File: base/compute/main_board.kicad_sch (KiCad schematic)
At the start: 18 parts, among them J1 USB_C_Receptacle_USB2.0_16P, J3 Conn_02x20_Counter_Clockwise, U1 MCP1700T-1202ETT, U3 LD1117S33TR_SOT223

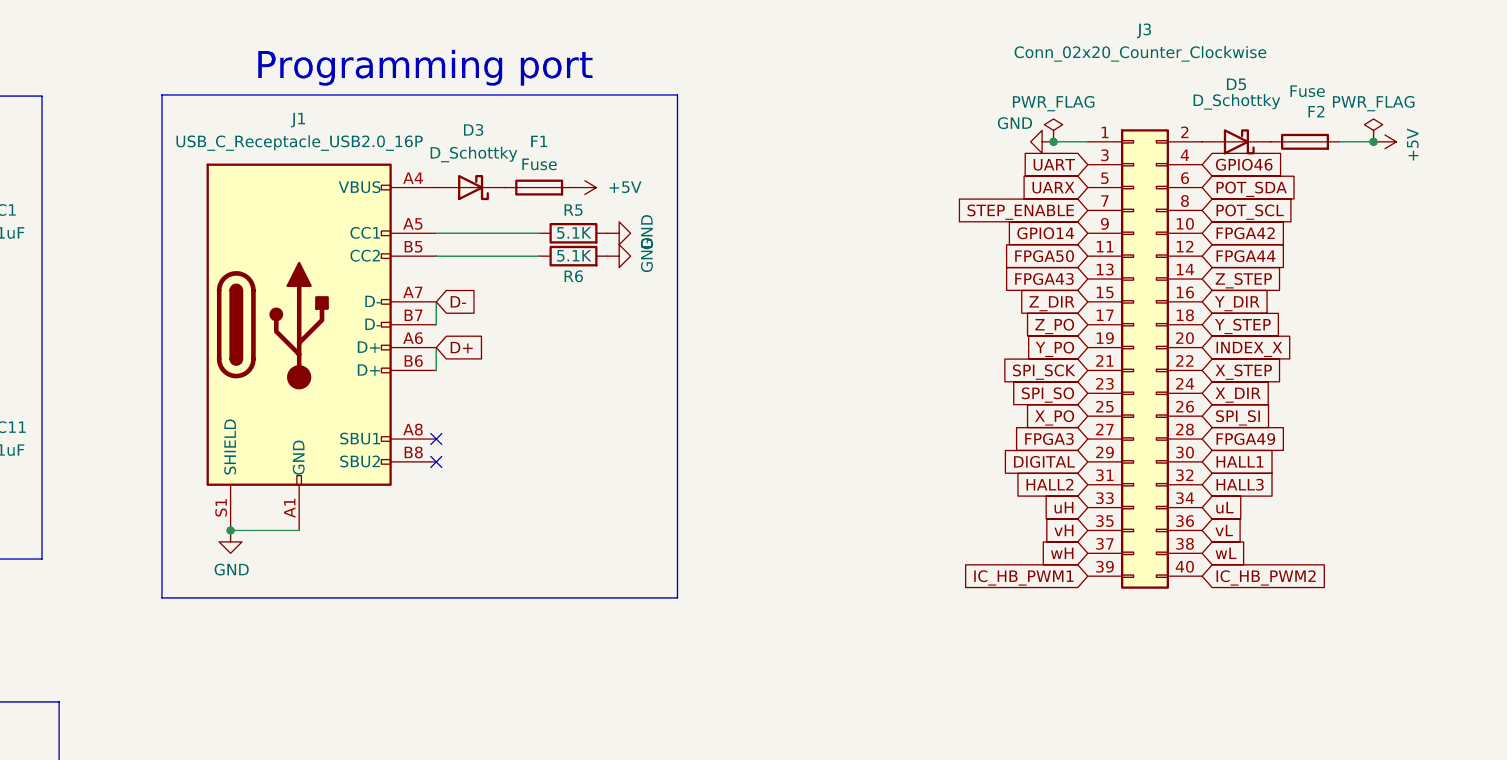
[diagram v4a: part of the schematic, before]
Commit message: fixed boms, small modifications to the boards.
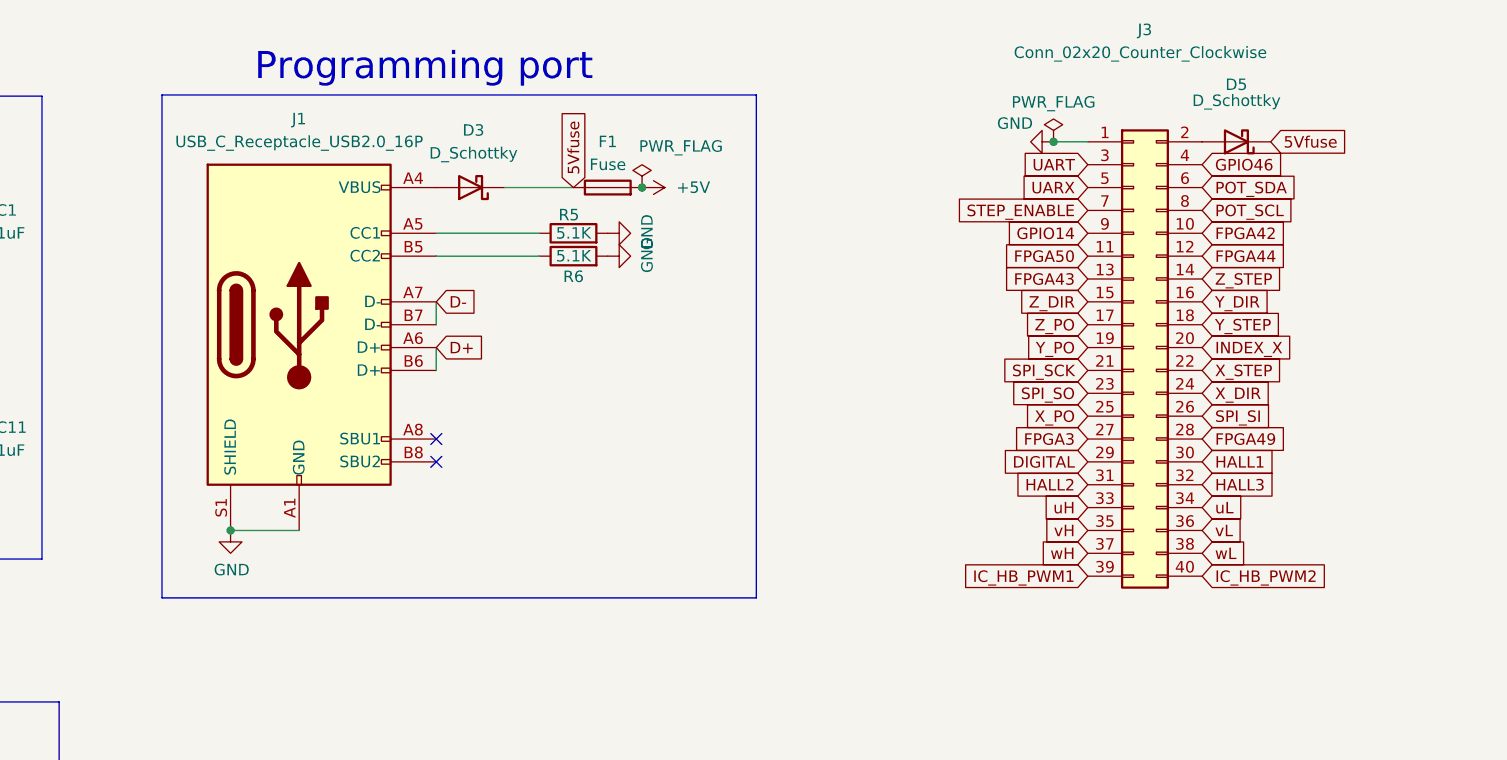
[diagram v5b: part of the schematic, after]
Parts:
- removed F2: Fuse, Fuse:Fuse_0402_1005Metric_Pad0.77x0.64mm_HandSolder, symbol Device:Fuse
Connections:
- net 5Vfuse: now reaches D5.1 (K)
- net 5Vfuse: now also D3.1 (K), F1.1
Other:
- moved on the sheet: F1
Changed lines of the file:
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@@
 	)
 	(junction
-		(at 121.92 77.47)
+		(at 167.64 39.37)
 		(diameter 0)
 		(color 0 0 0 0)
 	)
 	(junction
-		(at 248.92 34.29)
+		(at 121.92 77.47)
 		(diameter 0)
 		(color 0 0 0 0)
@@
 	(wire
 		(pts
-			(xy 248.92 34.29) (xy 245.11 34.29)
+			(xy 152.4 39.37) (xy 160.02 39.37)
 		)
 		(stroke
@@
 	(rectangle
 		(start 114.3 29.083)
-		(end 171.577 84.963)
+		(end 180.34 84.963)
 		(stroke
 			(width 0)
@@
 		)
 	)
+	(global_label "5Vfuse"
+		(shape input)
+		(at 237.49 34.29 0)
+		(fields_autoplaced yes)
+		(effects
+			(font
+				(size 1.27 1.27)
+			)
+			(justify left)
+		)
+		(property "Intersheetrefs" "${INTERSHEET_REFS}"
+			(at 246.1105 34.29 0)
+			(effects
+				(font
+					(size 1.27 1.27)
+				)
+				(justify left)
+				(hide yes)
+			)
+		)
+	)
+	(global_label "5Vfuse"
+		(shape input)
+		(at 160.02 39.37 90)
+		(fields_autoplaced yes)
+		(effects
+			(font
+				(size 1.27 1.27)
+			)
+			(justify left)
+		)
+		(property "Intersheetrefs" "${INTERSHEET_REFS}"
+			(at 160.02 30.7495 90)
+			(effects
+				(font
+					(size 1.27 1.27)
+				)
+				(justify left)
+				(hide yes)
+			)
+		)
+	)
 	(global_label "SPI_SO"
 		(shape input)
@@
 	)
 	(symbol
-		(lib_id "Device:Fuse")
-		(at 241.3 34.29 90)
-		(unit 1)
-		(exclude_from_sim no)
-		(in_bom yes)
-		(on_board yes)
-		(dnp no)
-		(property "Reference" "F2"
-			(at 242.57 30.988 90)
-			(effects
-				(font
-					(size 1.27 1.27)
-				)
-			)
-		)
-		(property "Value" "Fuse"
-			(at 241.554 28.702 90)
-			(effects
-				(font
-					(size 1.27 1.27)
-				)
-			)
-		)
-		(property "Footprint" "Fuse:Fuse_0402_1005Metric_Pad0.77x0.64mm_HandSolder"
-			(at 241.3 36.068 90)
-			(effects
-				(font
-					(size 1.27 1.27)
-				)
-				(hide yes)
-			)
-		)
-		(property "Datasheet" ""
-			(at 241.3 34.29 0)
-			(effects
-				(font
-					(size 1.27 1.27)
-				)
-				(hide yes)
-			)
-		)
-		(property "Description" ""
-			(at 241.3 34.29 0)
-			(effects
-				(font
-					(size 1.27 1.27)
-				)
-				(hide yes)
-			)
-		)
-		(property "farnell#" "2799448"
-			(at 241.3 34.29 90)
-			(effects
-				(font
-					(size 1.27 1.27)
-				)
-				(hide yes)
-			)
-		)
-		(property "manf#" "SF-0402FP100-2"
-			(at 241.3 34.29 90)
-			(effects
-				(font
-					(size 1.27 1.27)
-				)
-				(hide yes)
-			)
-		)
-		(property "mouser#" "652-SF-0402FP100-2"
-			(at 241.3 34.29 90)
-			(effects
-				(font
-					(size 1.27 1.27)
-				)
-				(hide yes)
-			)
-		)
-		(pin "1"
-		)
-		(pin "2"
-		)
-		(instances
-			(project "main_board"
-				(path "/3f5fe6b7-98fc-4d3e-9567-f9f7202d1455"
-					(reference "F2")
-					(unit 1)
-				)
-			)
-		)
-	)
-	(symbol
 		(lib_id "Device:LED_ABGR")
 		(at 82.55 113.03 180)
@@
 		(dnp no)
 		(property "Reference" "R5"
-			(at 160.02 41.91 90)
+			(at 159.512 42.418 90)
 			(effects
 				(font
@@
 	)
 	(symbol
-		(lib_id "power:+5V")
-		(at 248.92 34.29 270)
-		(unit 1)
-		(exclude_from_sim no)
-		(in_bom yes)
-		(on_board yes)
-		(dnp no)
-		(property "Reference" "#PWR01"
-			(at 245.11 34.29 0)
-			(effects
-				(font
-					(size 1.27 1.27)
-				)
-				(hide yes)
-			)
-		)
-		(property "Value" "+5V"
-			(at 253.3142 34.671 0)
-			(effects
-				(font
-					(size 1.27 1.27)
-				)
-			)
-		)
-		(property "Footprint" ""
-			(at 248.92 34.29 0)
-			(effects
-				(font
-					(size 1.27 1.27)
-				)
-				(hide yes)
-			)
-		)
-		(property "Datasheet" ""
-			(at 248.92 34.29 0)
-			(effects
-				(font
-					(size 1.27 1.27)
-				)
-				(hide yes)
-			)
-		)
-		(property "Description" "Power symbol creates a global label with name \"+5V\""
-			(at 248.92 34.29 0)
-			(effects
-				(font
-					(size 1.27 1.27)
-				)
-				(hide yes)
-			)
-		)
-		(pin "1"
-		)
-		(instances
-			(project "main_board"
-				(path "/3f5fe6b7-98fc-4d3e-9567-f9f7202d1455"
-					(reference "#PWR01")
-					(unit 1)
-				)
-			)
-		)
-	)
-	(symbol
 		(lib_id "Device:Fuse")
-		(at 156.21 39.37 90)
+		(at 163.83 39.37 90)
 		(unit 1)
 		(exclude_from_sim no)
@@
 		(fields_autoplaced yes)
 		(property "Reference" "F1"
-			(at 156.21 34.29 90)
+			(at 163.83 34.29 90)
 			(effects
 				(font
@@
 		)
 		(property "Value" "Fuse"
-			(at 156.21 36.83 90)
+			(at 163.83 36.83 90)
 			(effects
 				(font
@@
 		)
 		(property "Footprint" "Fuse:Fuse_0402_1005Metric_Pad0.77x0.64mm_HandSolder"
-			(at 156.21 41.148 90)
+			(at 163.83 41.148 90)
 			(effects
 				(font
@@
 		)
 		(property "Datasheet" ""
-			(at 156.21 39.37 0)
+			(at 163.83 39.37 0)
 			(effects
 				(font
@@
 		)
 		(property "Description" ""
-			(at 156.21 39.37 0)
+			(at 163.83 39.37 0)
 			(effects
 				(font
@@
 		)
 		(property "farnell#" "2799448"
-			(at 156.21 39.37 90)
+			(at 163.83 39.37 90)
 			(effects
 				(font
@@
 		)
 		(property "manf#" "SF-0402FP100-2"
-			(at 156.21 39.37 90)
+			(at 163.83 39.37 90)
 			(effects
 				(font
@@
 		)
 		(property "mouser#" "652-SF-0402FP100-2"
-			(at 156.21 39.37 90)
+			(at 163.83 39.37 90)
 			(effects
 				(font
@@
 	(symbol
 		(lib_id "power:PWR_FLAG")
-		(at 248.92 34.29 0)
+		(at 167.64 39.37 0)
 		(unit 1)
 		(exclude_from_sim no)
@@
 		(dnp no)
 		(property "Reference" "#FLG02"
-			(at 248.92 32.385 0)
+			(at 167.64 37.465 0)
 			(effects
 				(font
@@
 		)
 		(property "Value" "PWR_FLAG"
-			(at 248.92 29.8958 0)
+			(at 171.958 34.798 0)
 			(effects
 				(font
@@
 		)
 		(property "Footprint" ""
-			(at 248.92 34.29 0)
+			(at 167.64 39.37 0)
 			(effects
 				(font
@@
 		)
 		(property "Datasheet" "~"
-			(at 248.92 34.29 0)
+			(at 167.64 39.37 0)
 			(effects
 				(font
@@
 		)
 		(property "Description" "Special symbol for telling ERC where power comes from"
-			(at 248.92 34.29 0)
+			(at 167.64 39.37 0)
 			(effects
 				(font
@@
 	(symbol
 		(lib_id "power:+5V")
-		(at 160.02 39.37 270)
+		(at 167.64 39.37 270)
 		(unit 1)
 		(exclude_from_sim no)
@@
 		(dnp no)
 		(property "Reference" "#PWR03"
-			(at 156.21 39.37 0)
+			(at 163.83 39.37 0)
 			(effects
 				(font
@@
 		)
 		(property "Value" "+5V"
-			(at 163.83 39.37 90)
+			(at 171.45 39.37 90)
 			(effects
 				(font
@@
 		)
 		(property "Footprint" ""
-			(at 160.02 39.37 0)
+			(at 167.64 39.37 0)
 			(effects
 				(font
@@
 		)
 		(property "Datasheet" ""
-			(at 160.02 39.37 0)
+			(at 167.64 39.37 0)
 			(effects
 				(font
@@
 		)
 		(property "Description" "Power symbol creates a global label with name \"+5V\""
-			(at 160.02 39.37 0)
+			(at 167.64 39.37 0)
 			(effects
 				(font

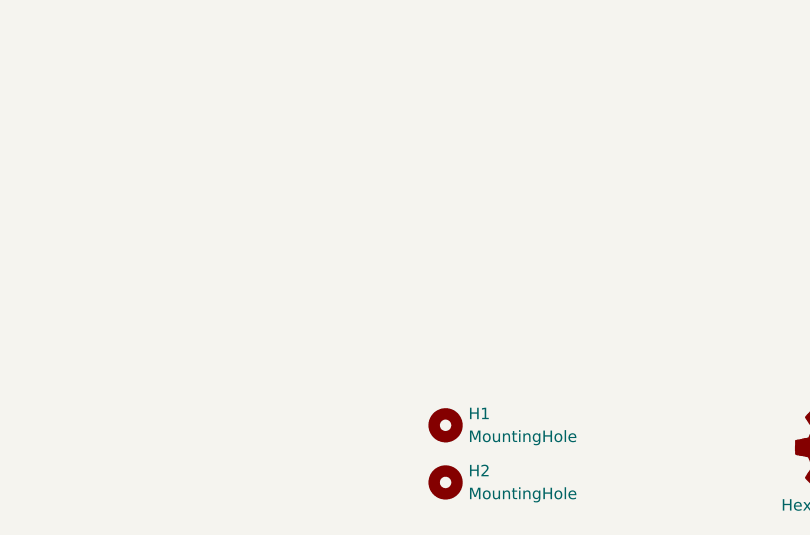
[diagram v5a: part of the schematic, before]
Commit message: added pcb files, added offset between compute and extension
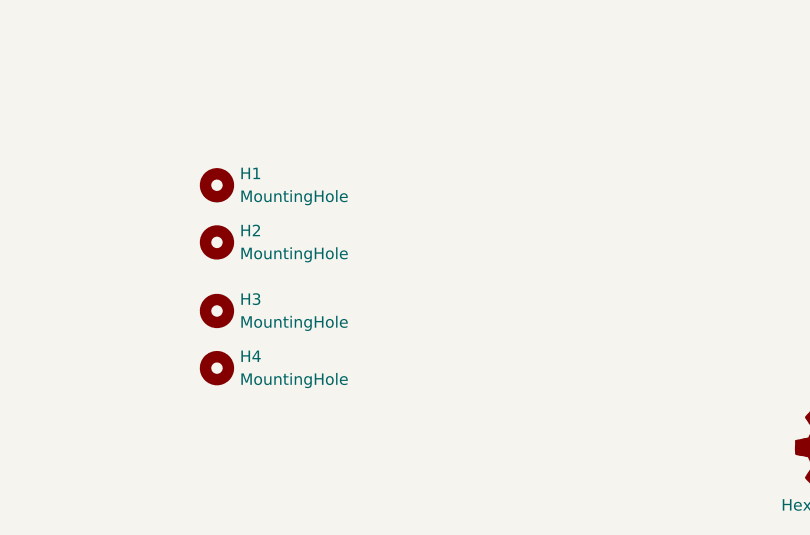
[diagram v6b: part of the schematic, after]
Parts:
- added H3, H4: MountingHole, MountingHole:MountingHole_2.2mm_M2, symbol Mechanical:MountingHole
- H1, H2: footprint MountingHole:MountingHole_3.2mm_M3 -> MountingHole:MountingHole_2.2mm_M2
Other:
- moved on the sheet: H1, H2
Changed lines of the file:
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@@
 	(symbol
 		(lib_id "Mechanical:MountingHole")
-		(at 208.28 148.59 0)
+		(at 182.88 121.92 0)
 		(unit 1)
 		(exclude_from_sim yes)
@@
 		(fields_autoplaced yes)
 		(property "Reference" "H2"
-			(at 210.82 147.3199 0)
+			(at 185.42 120.6499 0)
 			(effects
 				(font
@@
 		)
 		(property "Value" "MountingHole"
-			(at 210.82 149.8599 0)
+			(at 185.42 123.1899 0)
 			(effects
 				(font
@@
 			)
 		)
-		(property "Footprint" "MountingHole:MountingHole_3.2mm_M3"
-			(at 208.28 148.59 0)
+		(property "Footprint" "MountingHole:MountingHole_2.2mm_M2"
+			(at 182.88 121.92 0)
 			(effects
 				(font
@@
 		)
 		(property "Datasheet" "~"
-			(at 208.28 148.59 0)
+			(at 182.88 121.92 0)
 			(effects
 				(font
@@
 		)
 		(property "Description" "Mounting Hole without connection"
-			(at 208.28 148.59 0)
+			(at 182.88 121.92 0)
 			(effects
 				(font
@@
 	(symbol
 		(lib_id "Mechanical:MountingHole")
-		(at 208.28 142.24 0)
+		(at 182.88 129.54 0)
 		(unit 1)
 		(exclude_from_sim yes)
@@
 		(dnp no)
 		(fields_autoplaced yes)
+		(property "Reference" "H3"
+			(at 185.42 128.2699 0)
+			(effects
+				(font
+					(size 1.27 1.27)
+				)
+				(justify left)
+			)
+		)
+		(property "Value" "MountingHole"
+			(at 185.42 130.8099 0)
+			(effects
+				(font
+					(size 1.27 1.27)
+				)
+				(justify left)
+			)
+		)
+		(property "Footprint" "MountingHole:MountingHole_2.2mm_M2"
+			(at 182.88 129.54 0)
+			(effects
+				(font
+					(size 1.27 1.27)
+				)
+				(hide yes)
+			)
+		)
+		(property "Datasheet" "~"
+			(at 182.88 129.54 0)
+			(effects
+				(font
+					(size 1.27 1.27)
+				)
+				(hide yes)
+			)
+		)
+		(property "Description" "Mounting Hole without connection"
+			(at 182.88 129.54 0)
+			(effects
+				(font
+					(size 1.27 1.27)
+				)
+				(hide yes)
+			)
+		)
+		(instances
+			(project "main_board"
+				(path "/3f5fe6b7-98fc-4d3e-9567-f9f7202d1455"
+					(reference "H3")
+					(unit 1)
+				)
+			)
+		)
+	)
+	(symbol
+		(lib_id "Mechanical:MountingHole")
+		(at 182.88 115.57 0)
+		(unit 1)
+		(exclude_from_sim yes)
+		(in_bom no)
+		(on_board yes)
+		(dnp no)
+		(fields_autoplaced yes)
 		(property "Reference" "H1"
-			(at 210.82 140.9699 0)
+			(at 185.42 114.2999 0)
 			(effects
 				(font
@@
 		)
 		(property "Value" "MountingHole"
-			(at 210.82 143.5099 0)
+			(at 185.42 116.8399 0)
 			(effects
 				(font
@@
 			)
 		)
-		(property "Footprint" "MountingHole:MountingHole_3.2mm_M3"
-			(at 208.28 142.24 0)
+		(property "Footprint" "MountingHole:MountingHole_2.2mm_M2"
+			(at 182.88 115.57 0)
 			(effects
 				(font
@@
 		)
 		(property "Datasheet" "~"
-			(at 208.28 142.24 0)
+			(at 182.88 115.57 0)
 			(effects
 				(font
@@
 		)
 		(property "Description" "Mounting Hole without connection"
-			(at 208.28 142.24 0)
+			(at 182.88 115.57 0)
 			(effects
 				(font
@@
 					(unit 1)
 				)
+			)
+		)
+	)
+	(symbol
+		(lib_id "Mechanical:MountingHole")
+		(at 182.88 135.89 0)
+		(unit 1)
+		(exclude_from_sim yes)
+		(in_bom no)
+		(on_board yes)
+		(dnp no)
+		(fields_autoplaced yes)
+		(property "Reference" "H4"
+			(at 185.42 134.6199 0)
+			(effects
+				(font
+					(size 1.27 1.27)
+				)
+				(justify left)
+			)
+		)
+		(property "Value" "MountingHole"
+			(at 185.42 137.1599 0)
+			(effects
+				(font
+					(size 1.27 1.27)
+				)
+				(justify left)
+			)
+		)
+		(property "Footprint" "MountingHole:MountingHole_2.2mm_M2"
+			(at 182.88 135.89 0)
+			(effects
+				(font
+					(size 1.27 1.27)
+				)
+				(hide yes)
+			)
+		)
+		(property "Datasheet" "~"
+			(at 182.88 135.89 0)
+			(effects
+				(font
+					(size 1.27 1.27)
+				)
+				(hide yes)
+			)
+		)
+		(property "Description" "Mounting Hole without connection"
+			(at 182.88 135.89 0)
+			(effects
+				(font
+					(size 1.27 1.27)
+				)
+				(hide yes)
+			)
+		)
+		(instances
+			(project "main_board"
+				(path "/3f5fe6b7-98fc-4d3e-9567-f9f7202d1455"
+					(reference "H4")
+					(unit 1)
+				)
